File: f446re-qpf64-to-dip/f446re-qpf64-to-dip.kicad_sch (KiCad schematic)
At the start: 3 parts, among them J1 Conn_01x32_Pin, J2 Conn_01x32_Pin, U1 STM32F446RETx

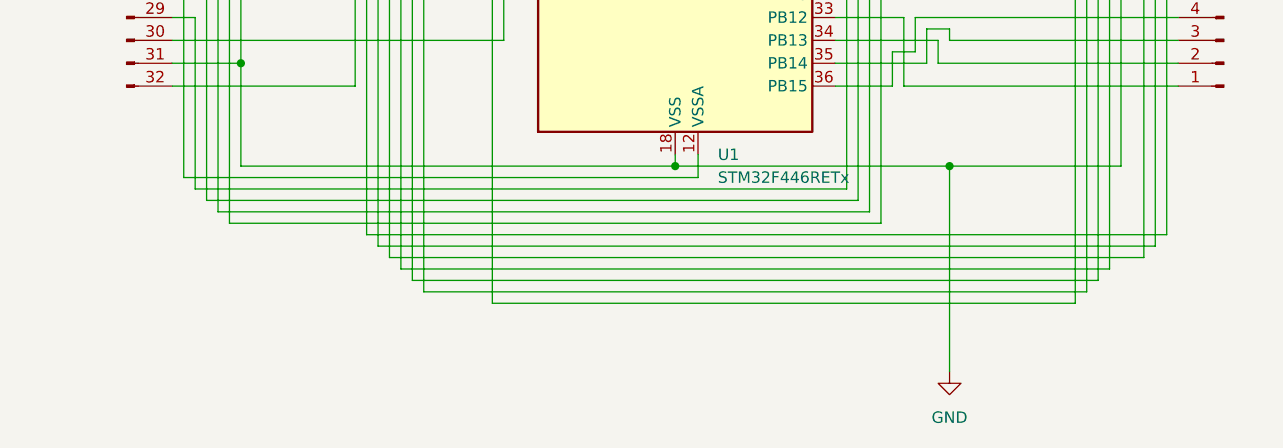
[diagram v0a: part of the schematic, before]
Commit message: change: 基盤サイズ変更
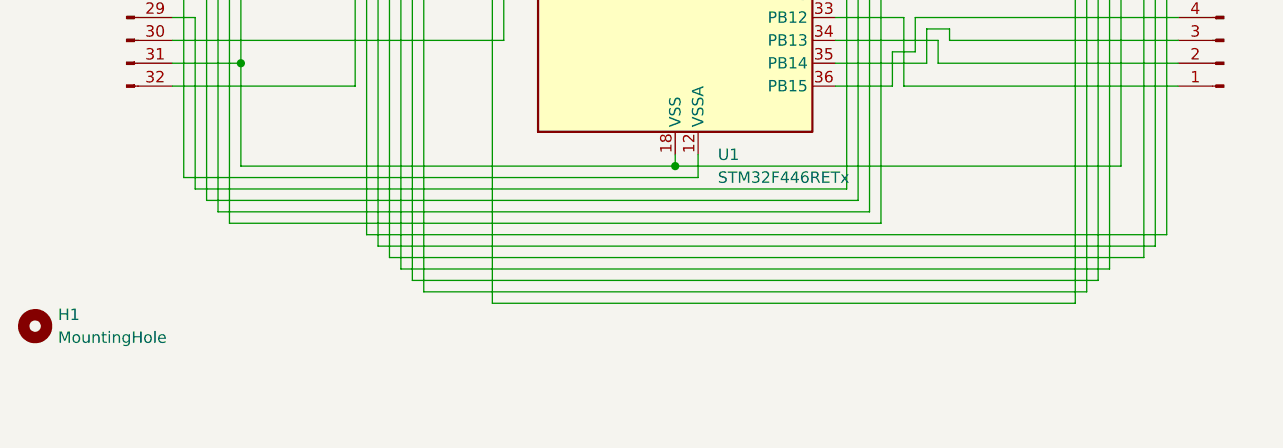
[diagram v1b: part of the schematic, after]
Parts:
- added H1: MountingHole, MountingHole:MountingHole_3.2mm_M3, symbol Mechanical:MountingHole
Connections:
- net GND: no longer names the net of J1.18 (Pin_18), J1.31 (Pin_31), J2.15 (Pin_15), J2.31 (Pin_31), U1.18 (VSS), U1.31 (VSS), U1.47 (VSS), U1.63 (VSS)
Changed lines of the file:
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@@
-	)
-	(junction
-		(at 149.86 138.43)
-		(diameter 0)
-		(color 0 0 0 0)
 	)
 	(junction
@@
 	(wire
 		(pts
-			(xy 119.38 138.43) (xy 149.86 138.43)
-		)
-		(stroke
-			(width 0)
-			(type default)
-		)
-	)
-	(wire
-		(pts
 			(xy 137.16 50.8) (xy 147.32 50.8)
 		)
@@
 	(wire
 		(pts
-			(xy 149.86 138.43) (xy 168.91 138.43)
+			(xy 119.38 138.43) (xy 168.91 138.43)
 		)
 		(stroke
@@
 		(pts
 			(xy 101.6 116.84) (xy 100.33 116.84)
-		)
-		(stroke
-			(width 0)
-			(type default)
-		)
-	)
-	(wire
-		(pts
-			(xy 149.86 138.43) (xy 149.86 161.29)
 		)
 		(stroke
@@
 	)
 	(symbol
+		(lib_id "Mechanical:MountingHole")
+		(at 48.26 156.21 0)
+		(unit 1)
+		(exclude_from_sim yes)
+		(in_bom no)
+		(on_board yes)
+		(dnp no)
+		(fields_autoplaced yes)
+		(property "Reference" "H1"
+			(at 50.8 154.9399 0)
+			(effects
+				(font
+					(size 1.27 1.27)
+				)
+				(justify left)
+			)
+		)
+		(property "Value" "MountingHole"
+			(at 50.8 157.4799 0)
+			(effects
+				(font
+					(size 1.27 1.27)
+				)
+				(justify left)
+			)
+		)
+		(property "Footprint" "MountingHole:MountingHole_3.2mm_M3"
+			(at 48.26 156.21 0)
+			(effects
+				(font
+					(size 1.27 1.27)
+				)
+				(hide yes)
+			)
+		)
+		(property "Datasheet" "~"
+			(at 48.26 156.21 0)
+			(effects
+				(font
+					(size 1.27 1.27)
+				)
+				(hide yes)
+			)
+		)
+		(property "Description" "Mounting Hole without connection"
+			(at 48.26 156.21 0)
+			(effects
+				(font
+					(size 1.27 1.27)
+				)
+				(hide yes)
+			)
+		)
+		(instances
+			(project ""
+				(path "/be5b2ad2-ca8a-407e-bbd9-7815341ce36a"
+					(reference "H1")
+					(unit 1)
+				)
+			)
+		)
+	)
+	(symbol
 		(lib_id "MCU_ST_STM32F4:STM32F446RETx")
 		(at 119.38 91.44 0)
@@
 					(unit 1)
 				)
-			)
-		)
-	)
-	(symbol
-		(lib_id "power:GND")
-		(at 149.86 161.29 0)
-		(unit 1)
-		(exclude_from_sim no)
-		(in_bom yes)
-		(on_board yes)
-		(dnp no)
-		(property "Reference" "#PWR01"
-			(at 149.86 167.64 0)
-			(effects
-				(font
-					(size 1.27 1.27)
-				)
-				(hide yes)
-			)
-		)
-		(property "Value" "GND"
-			(at 149.86 166.37 0)
-			(effects
-				(font
-					(size 1.27 1.27)
-				)
-			)
-		)
-		(property "Footprint" ""
-			(at 149.86 161.29 0)
-			(effects
-				(font
-					(size 1.27 1.27)
-				)
-				(hide yes)
-			)
-		)
-		(property "Datasheet" ""
-			(at 149.86 161.29 0)
-			(effects
-				(font
-					(size 1.27 1.27)
-				)
-				(hide yes)
-			)
-		)
-		(property "Description" "Power symbol creates a global label with name \"GND\" , ground"
-			(at 149.86 161.29 0)
-			(effects
-				(font
-					(size 1.27 1.27)
-				)
-				(hide yes)
-			)
-		)
-		(pin "1"
-		)
-		(instances
-			(project ""
-				(path "/be5b2ad2-ca8a-407e-bbd9-7815341ce36a"
-					(reference "#PWR01")
-					(unit 1)
-				)
